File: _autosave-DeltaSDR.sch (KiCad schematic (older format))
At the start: 59 parts, among them J1 Conn_01x03_Male, J2 Conn_01x05_Male, J3 Barrel_Jack, J4 USB_A, J6 Conn_01x02_Male, Q7 MMBT3904, U1 MCP1703T-3302E/DB, U2 Si570, U4 PCM3060, U5 CY8C3246PVI-147, U6 MCP1703T-5002E/DB, U7 MCP1703T-5002E/DB, U8 74HC74, Y1 Crystal_GND24

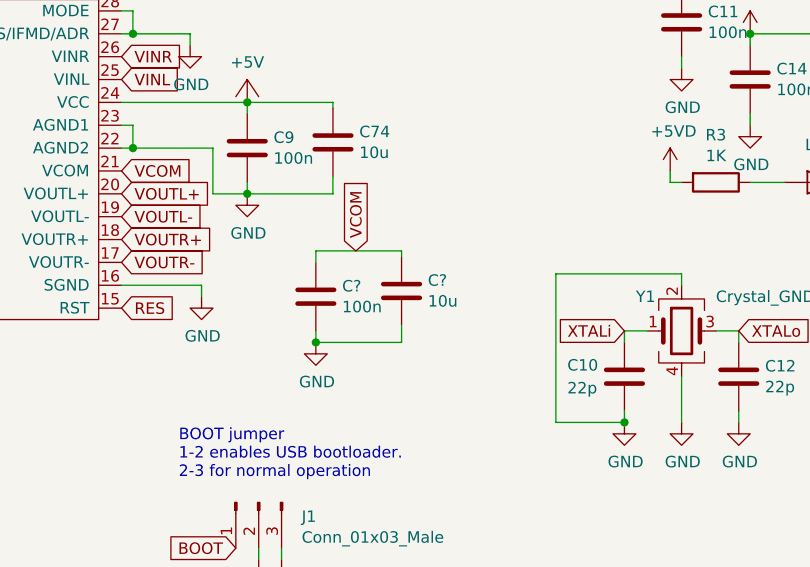
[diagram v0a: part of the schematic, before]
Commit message: Added capacitors to codec's VCOM
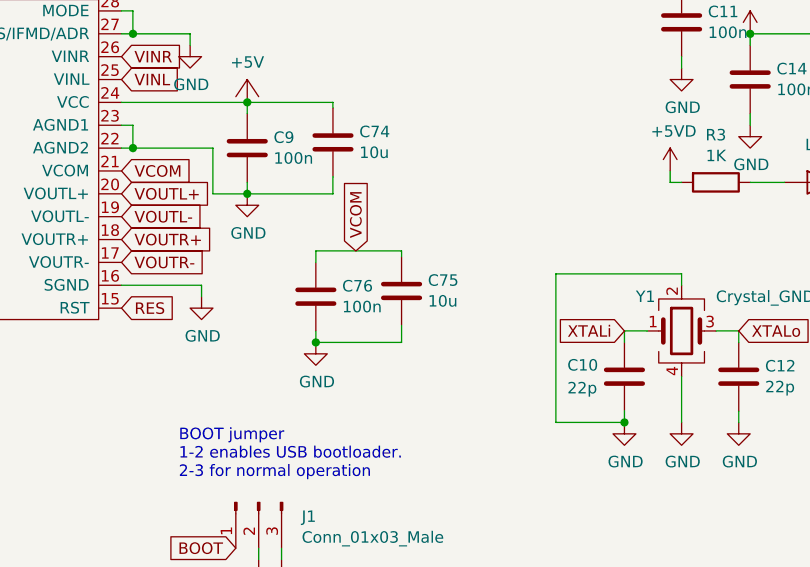
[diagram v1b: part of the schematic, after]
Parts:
- gave numbers to parts that had none: 2
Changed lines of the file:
@@
 D-
 $Comp
-L DeltaSDR-rescue:C-Device-DeltaSDR-rescue C?
+L DeltaSDR-rescue:C-Device-DeltaSDR-rescue C76
 U 1 1 5F664756
 P 4950 5050
-F 0 "C?" H 5065 5096 50  0000 L CNN
+F 0 "C76" H 5065 5096 50  0000 L CNN
 F 1 "100n" H 5065 5005 50  0000 L CNN
 F 2 "Capacitor_SMD:C_0603_1608Metric" H 4988 4900 50  0001 C CNN
@@
 	4950 4850 4950 4900
 $Comp
-L power:GND #PWR?
+L power:GND #PWR0232
 U 1 1 5F664761
 P 4950 5250
-F 0 "#PWR?" H 4950 5000 50  0001 C CNN
+F 0 "#PWR0232" H 4950 5000 50  0001 C CNN
 F 1 "GND" H 4955 5077 50  0000 C CNN
 F 2 "" H 4950 5250 50  0001 C CNN
@@
 Connection ~ 4950 5250
 $Comp
-L DeltaSDR-rescue:C-Device-DeltaSDR-rescue C?
+L DeltaSDR-rescue:C-Device-DeltaSDR-rescue C75
 U 1 1 5F66477A
 P 5325 5025
-F 0 "C?" H 5440 5071 50  0000 L CNN
+F 0 "C75" H 5440 5071 50  0000 L CNN
 F 1 "10u" H 5440 4980 50  0000 L CNN
 F 2 "Capacitor_SMD:C_0805_2012Metric" H 5363 4875 50  0001 C CNN
